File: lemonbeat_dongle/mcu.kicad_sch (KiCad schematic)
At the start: 42 parts, among them J201 USB_A, J202 Prog, J203 u.FL, SW201 SW_Push, U201 nRF52840, Y201 32MHz, Y202 32.768kHz

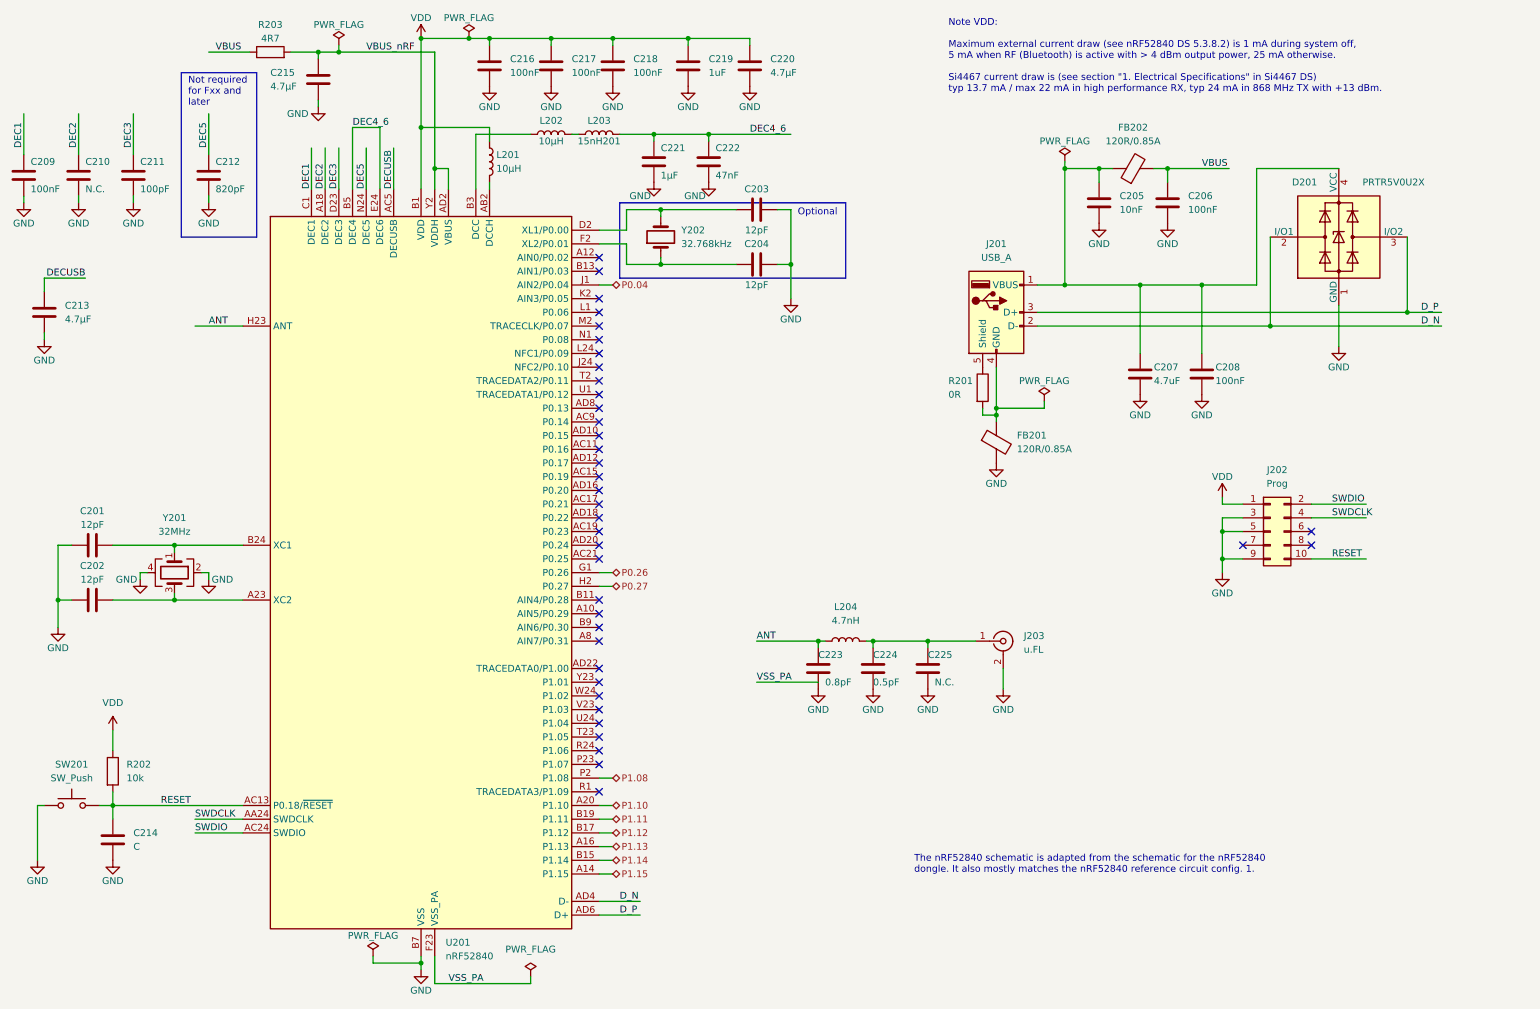
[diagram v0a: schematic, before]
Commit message: lemonbeat dongle: assign footprints & add LCSC part numbers
Needs to be double-checked.
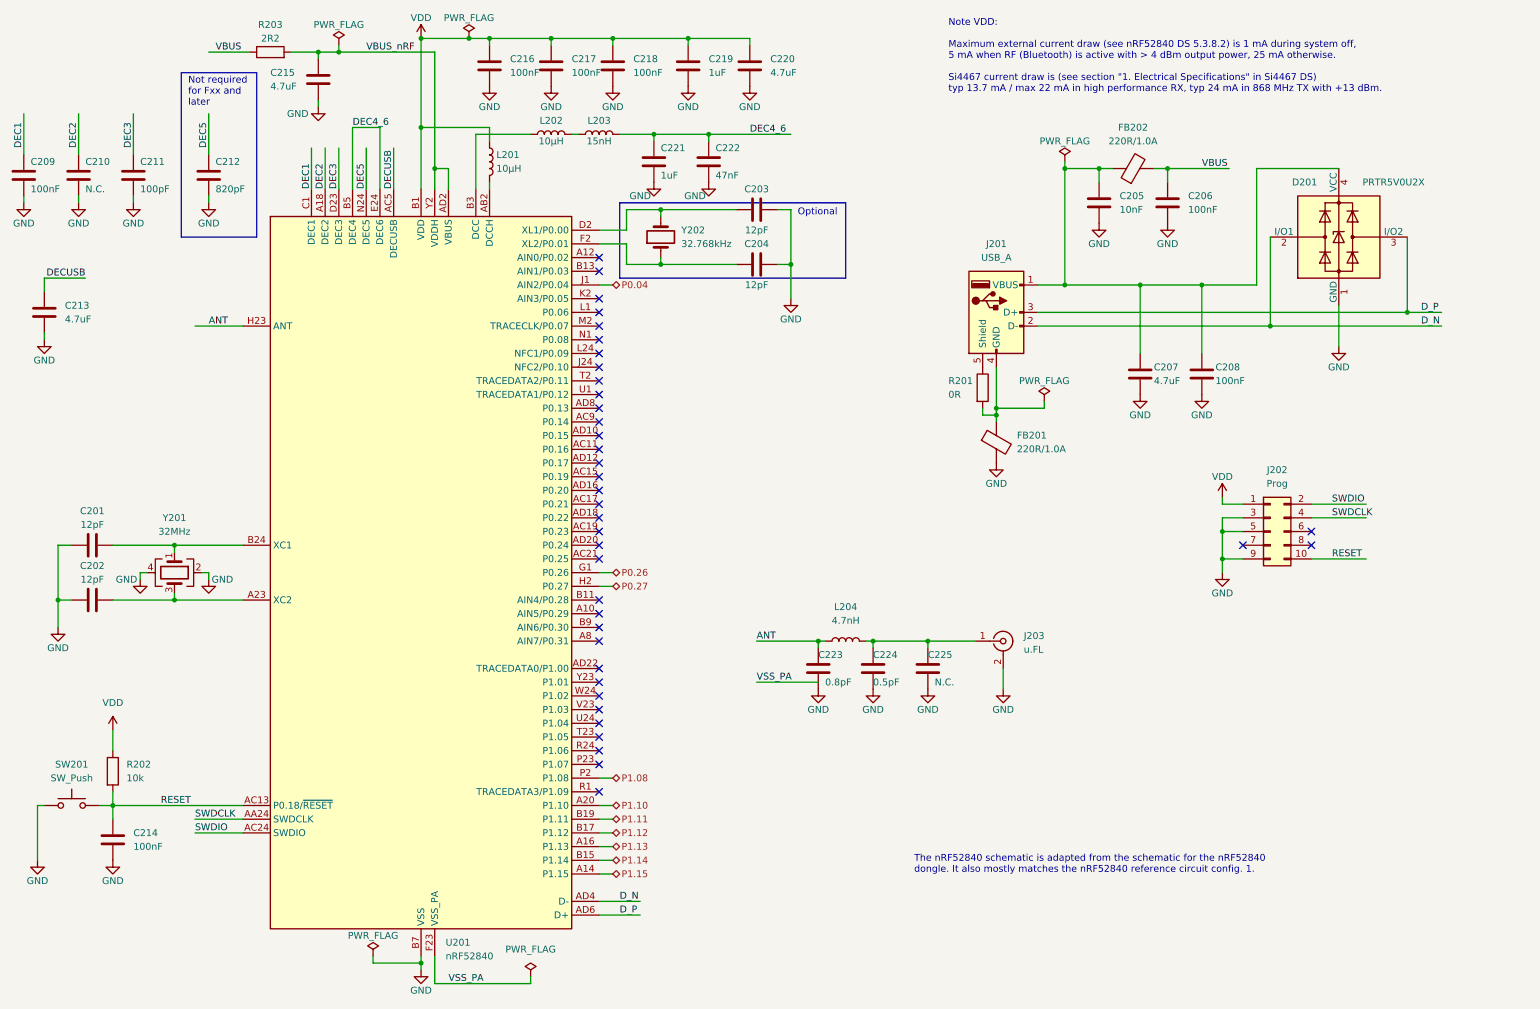
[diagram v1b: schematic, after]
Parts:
- C201, C202, C203, C204: footprint (none) -> Resistor_SMD:R_0201_0603Metric; LCSC (none) -> C384960; Manufacturer (none) -> Murata Electronics; Part Number (none) -> GRM0335C1H120FA01D
- C205: footprint (none) -> Resistor_SMD:R_0201_0603Metric; LCSC (none) -> C85930; Manufacturer (none) -> Murata Electronics; Part Number (none) -> GRM033R71E103KE14D
- C206, C208, C209, C216, C217, C218: footprint (none) -> Resistor_SMD:R_0201_0603Metric; LCSC (none) -> C76939; Manufacturer (none) -> Murata Electronics; Part Number (none) -> GRM033R61E104KE14D
- C207: footprint (none) -> Resistor_SMD:R_0402_1005Metric; Comment (none) -> JLCPCB basic part; nRF52 dongle has ±20% 0402 here; LCSC (none) -> C23733; Manufacturer (none) -> Samsung Electro-Mechanics; Part Number (none) -> CL05A475MP5NRNC
- C210, C225: footprint (none) -> Resistor_SMD:R_0201_0603Metric
- C211: footprint (none) -> Resistor_SMD:R_0201_0603Metric; LCSC (none) -> C76922; Manufacturer (none) -> Murata Electronics; Part Number (none) -> GRM0335C1H101JA01D
- C212: footprint (none) -> Resistor_SMD:R_0201_0603Metric; Comment (none) -> Not required for nRF52840 Fxx and later; LCSC (none) -> C185597; Manufacturer (none) -> Murata Electronics; Part Number (none) -> GRM033R71E821KA01D
- C213, C220: value 4.7μF -> 4.7uF; footprint (none) -> Resistor_SMD:R_0603_1608Metric; Comment (none) -> JLCPCB basic part; nRF52 dongle has ±10% 0603 here; LCSC (none) -> C19666; Manufacturer (none) -> Samsung Electro-Mechanics; Part Number (none) -> CL10A475KO8NNNC
- C214: value C -> 100nF; footprint (none) -> Resistor_SMD:R_0201_0603Metric; LCSC (none) -> C76939; Manufacturer (none) -> Murata Electronics; Part Number (none) -> GRM033R61E104KE14D
- C215: value 4.7μF -> 4.7uF; footprint (none) -> Resistor_SMD:R_0402_1005Metric; Comment (none) -> JLCPCB basic part; nRF52 dongle has ±20% 0402 here; LCSC (none) -> C23733; Manufacturer (none) -> Samsung Electro-Mechanics; Part Number (none) -> CL05A475MP5NRNC
- C219: footprint (none) -> Resistor_SMD:R_0603_1608Metric; Comment (none) -> JLCPCB basic part; LCSC (none) -> C15849; Manufacturer (none) -> Samsung Electro-Mechanics; Part Number (none) -> CL10A105KB8NNNC
- C221: value 1μF -> 1uF; footprint (none) -> Resistor_SMD:R_0603_1608Metric; Comment (none) -> JLCPCB basic part; LCSC (none) -> C15849; Manufacturer (none) -> Samsung Electro-Mechanics; Part Number (none) -> CL10A105KB8NNNC
- C222: footprint (none) -> Resistor_SMD:R_0201_0603Metric; LCSC (none) -> C126621; Manufacturer (none) -> Murata Electronics; Part Number (none) -> GRT033R60J473KE01D
- C223: footprint (none) -> Resistor_SMD:R_0201_0603Metric; LCSC (none) -> C161294; Manufacturer (none) -> Murata Electronics; Part Number (none) -> GJM0335C1ER80BB01D
- C224: footprint (none) -> Resistor_SMD:R_0201_0603Metric; LCSC (none) -> C85920; Manufacturer (none) -> Murata Electronics; Part Number (none) -> GRM0335C1HR50BA01D
- FB201, FB202: value 120R/0.85A -> 220R/1.0A; footprint (none) -> Resistor_SMD:R_0402_1005Metric; Comment (none) -> nRF52 dongle uses Taiyo Yuden BKP0603HS121-T: Ferrite Bead,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; LCSC (none) -> C281196; Manufacturer (none) -> microgate; Part Number (none) -> MGLB1005M221T1R0-LF
- J201: footprint (none) -> Connector_USB:USB_A_CNCTech_1001-011-01101_Horizontal; Comment (none) -> Alternative at JLCPCB with same footprint: Molex 480371000 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; LCSC (none) -> C319178; Manufacturer (none) -> XKB Connectivity; Part Number (none) -> U217-041N-4BV81
- J202: footprint (none) -> Connector_PinHeader_1.27mm:PinHeader_2x05_P1.27mm_Vertical_SMD
- J203: footprint (none) -> Connector_Coaxial:U.FL_Hirose_U.FL-R-SMT-1_Vertical; LCSC (none) -> C88373; Manufacturer (none) -> Hirose; Part Number (none) -> U.FL-R-SMT-1(10)
- L201, L202: footprint (none) -> Inductor_SMD:L_0603_1608Metric; Comment (none) -> same part as nRF52 dongle; LCSC (none) -> C87216; Manufacturer (none) -> Taiyo Yuden; Part Number (none) -> LBMF1608T100K
- L203: renamed from 15nH201; value L203 -> 15nH; footprint (none) -> Inductor_SMD:L_0402_1005Metric; Comment (none) -> JLCPCB basic part; nRF52 dongle has 320mA, ±5%, 0402 (Taiyo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; LCSC (none) -> C27143; Manufacturer (none) -> Sunlord; Part Number (none) -> SDCL1005C15NJTDF
- L204: footprint (none) -> Inductor_SMD:L_0201_0603Metric; Comment (none) -> same part as nRF52 dongle; LCSC (none) -> C86126; Manufacturer (none) -> Murata Electronics; Part Number (none) -> LQP03TN4N7H02D
- R201: footprint (none) -> Resistor_SMD:R_0402_1005Metric; Comment (none) -> JLCPCB basic part; LCSC (none) -> C17168; Manufacturer (none) -> Uniroyal Elec; Part Number (none) -> 0402WGF0000TCE
- R202: footprint (none) -> Resistor_SMD:R_0402_1005Metric; Comment (none) -> JLCPCB basic part; LCSC (none) -> C25744; Manufacturer (none) -> Uniroyal Elec; Part Number (none) -> 0402WGF1002TCE
- R203: value 4R7 -> 2R2; footprint (none) -> Resistor_SMD:R_0201_0603Metric; LCSC (none) -> C247442; Manufacturer (none) -> Uniroyal Elec; Part Number (none) -> 0201WMF220KTCE
- SW201: footprint (none) -> Button_Switch_SMD:SW_SPST_PTS810; LCSC (none) -> C221896; Manufacturer (none) -> C&K; Part Number (none) -> PTS810 SJK 250 SMTR LFS
- U201: LCSC (none) -> C190794; Manufacturer (none) -> Nordic Semiconductor; Part Number (none) -> NRF52840-QIAA-R
- Y201: footprint (none) -> Crystal:Crystal_SMD_2016-4Pin_2.0x1.6mm
- Y202: footprint (none) -> Crystal:Crystal_SMD_3215-2Pin_3.2x1.5mm; LCSC (none) -> C32346; Manufacturer (none) -> Seiko Epson; Part Number (none) -> Q13FC1350000400

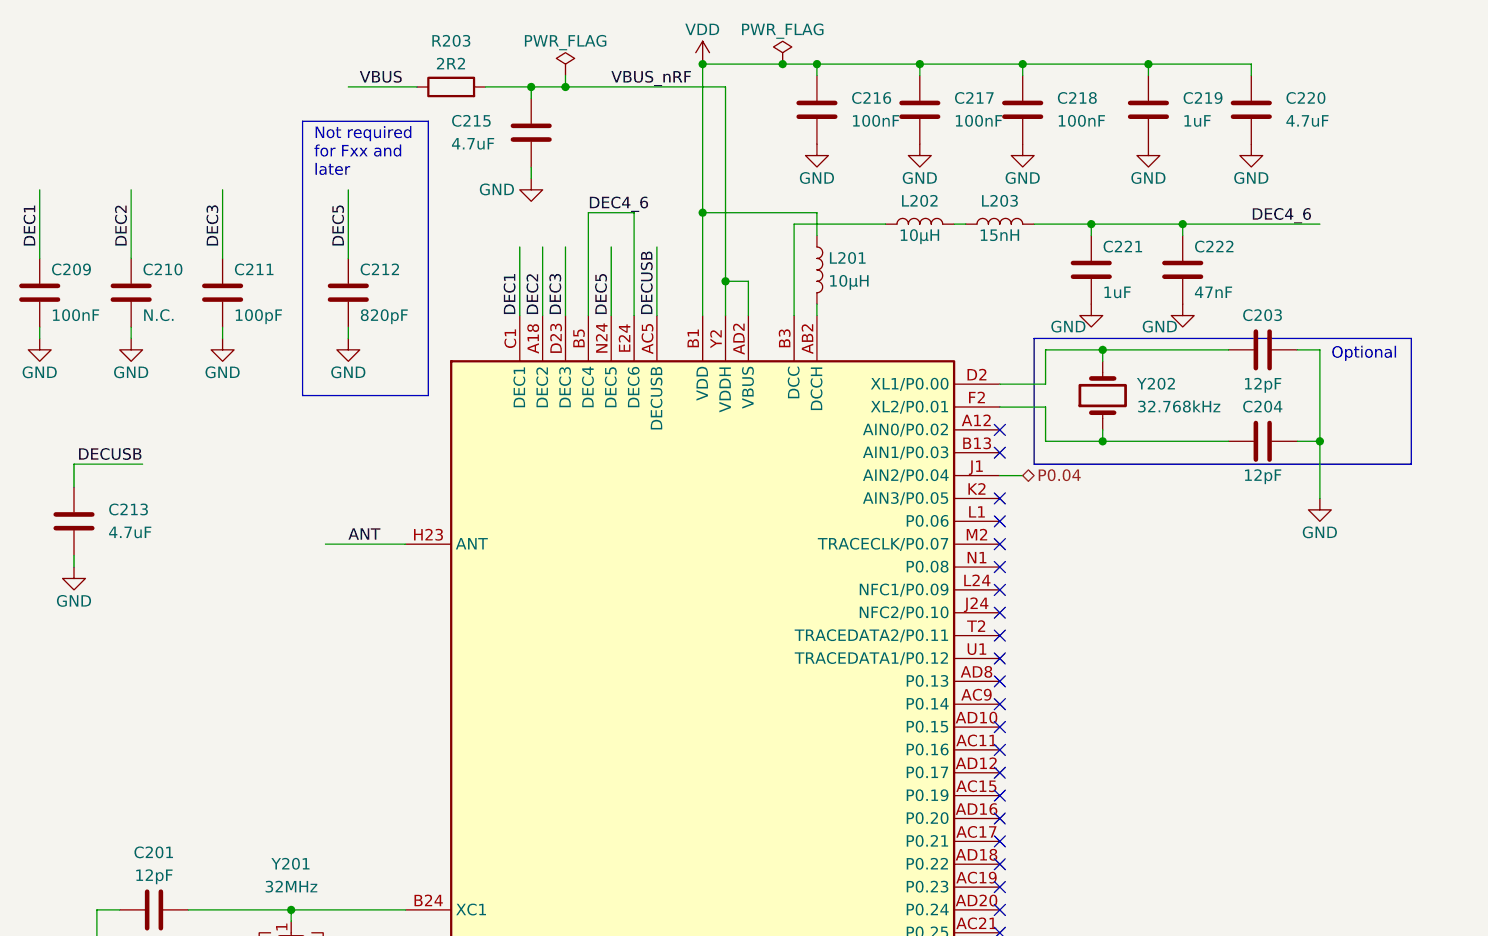
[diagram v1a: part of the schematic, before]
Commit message: dongle: remove inductors for DCC and DCCH
Inductors at DCC and DCCH are only needed when using the internal DCDC
regulators rather than the LDO regulators. Using the DCDC regulators
has the advantage of lower current consumption, but comes with several
disadvantages in this case:

- pins are on the inner ring of the nRF52840; this is not easily
  manufacturable at JLCPCB
- uses space on PCB (for this reason I have completely removed them
  rather than just not assembling them)
- significantly raises costs (each additional non-basic component
  incurs a 3$ setup fee)
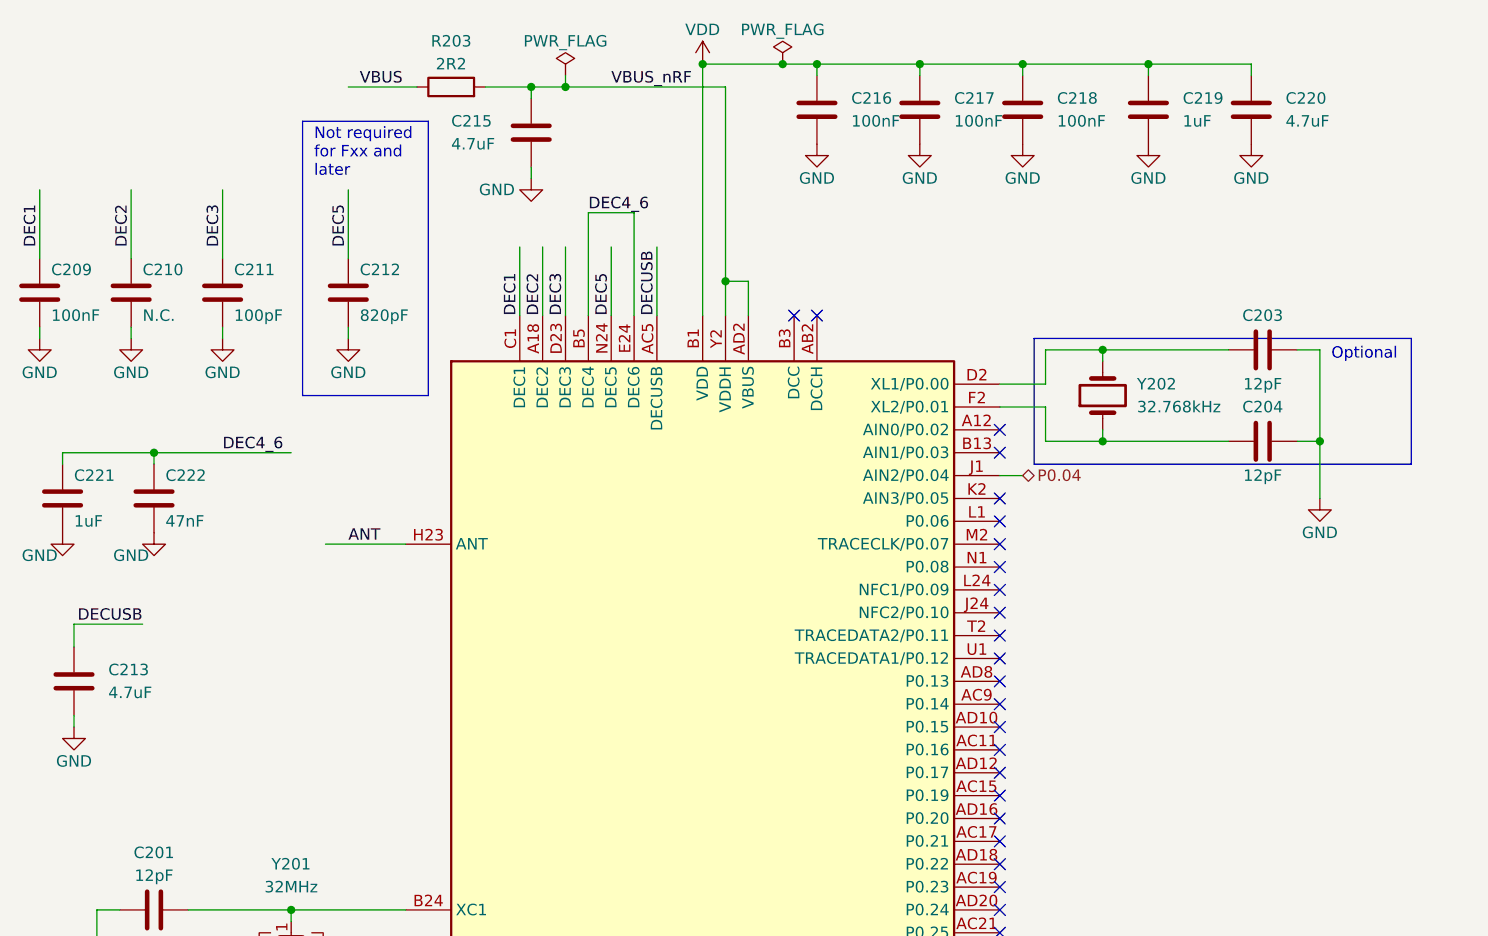
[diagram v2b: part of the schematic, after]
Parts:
- removed L201, L202: 10μH, Inductor_SMD:L_0603_1608Metric, symbol Device:L
- removed L203: 15nH, Inductor_SMD:L_0402_1005Metric, symbol Device:L
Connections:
- no-connect marks 38 -> 40
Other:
- moved on the sheet: C213, C221, C222

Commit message: donlge: mark C212 (1.3V regulator supply decoupling) as not in BOM
This part is N.C. on both nRF52 dongle and reference circuit.
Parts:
- C210: now left out of the parts list
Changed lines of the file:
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@@
   )
   (symbol (lib_id "Device:C") (at 25.4 44.45 0) (unit 1)
-    (in_bom yes) (on_board yes)
+    (in_bom no) (on_board yes)
     (property "Reference" "C210" (id 0) (at 26.67 41.91 0)
       (effects (font (size 1.27 1.27)) (justify left))

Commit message: dongle: mark C225 (at BLE RF output) as not in BOM
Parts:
- C225: now left out of the parts list
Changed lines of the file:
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@@
   )
   (symbol (lib_id "Device:C") (at 182.88 135.89 0) (unit 1)
-    (in_bom yes) (on_board yes)
+    (in_bom no) (on_board yes)
     (property "Reference" "C225" (id 0) (at 182.88 133.35 0)
       (effects (font (size 1.27 1.27)) (justify left))

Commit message: dongle: mark 32kHz crystal and capacitors as not in BOM
By default, LFCLK uses the RC oscillator (LFRC); LFXO is not needed
for the dongle.
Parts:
- C203, C204, Y202: now left out of the parts list
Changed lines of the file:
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@@
   )
   (symbol (lib_id "Device:C") (at 151.13 60.96 90) (unit 1)
-    (in_bom yes) (on_board yes)
+    (in_bom no) (on_board yes)
     (property "Reference" "C204" (id 0) (at 151.13 57.15 90))
     (property "Value" "12pF" (id 1) (at 151.13 64.77 90))
@@
   )
   (symbol (lib_id "Device:C") (at 151.13 50.8 270) (unit 1)
-    (in_bom yes) (on_board yes)
+    (in_bom no) (on_board yes)
     (property "Reference" "C203" (id 0) (at 151.13 46.99 90))
     (property "Value" "12pF" (id 1) (at 151.13 54.61 90))
@@
   )
   (symbol (lib_id "Device:Crystal") (at 133.35 55.88 90) (unit 1)
-    (in_bom yes) (on_board yes) (fields_autoplaced)
+    (in_bom no) (on_board yes) (fields_autoplaced)
     (property "Reference" "Y202" (id 0) (at 137.16 54.6099 90)
       (effects (font (size 1.27 1.27)) (justify right))

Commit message: dongle: mark C222 (additional decoupling at DEC4_6) as not in BOM
This capacitor is used in the nRF52 dongle schematic, but only exists
as N.C. component in the reference circuit.
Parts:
- C222: now left out of the parts list
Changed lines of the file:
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@@
   )
   (symbol (lib_id "Device:C") (at 27.94 67.31 0) (unit 1)
-    (in_bom yes) (on_board yes)
+    (in_bom no) (on_board yes)
     (property "Reference" "C222" (id 0) (at 29.21 64.77 0)
       (effects (font (size 1.27 1.27)) (justify left))
